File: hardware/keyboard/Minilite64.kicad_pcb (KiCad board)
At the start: 2 copper layers, 285.5 x 94.9 mm, 132 parts, among them J1 20P 1.0mm FFC ZIF bottom-cont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, SW1 Kailh MX hotswap / ~ / `, SW10 Kailh MX hotswap / ( / 9, SW11 Kailh MX hotswap / ) / 0, SW12 Kailh MX hotswap / _ / -, SW13 Kailh MX hotswap / + / =, SW14 Kailh MX hotswap / Backspace, SW15 Kailh MX hotswap / Tab, SW16 Kailh MX hotswap / Q, SW17 Kailh MX hotswap / W, SW18 Kailh MX hotswap / E, SW19 Kailh MX hotswap / R, SW2 Kailh MX hotswap / ! / 1, SW20 Kailh MX hotswap / T, SW21 Kailh MX hotswap / Y, SW22 Kailh MX hotswap / U, SW23 Kailh MX hotswap / I, SW24 Kailh MX hotswap / O, SW25 Kailh MX hotswap / P, SW26 Kailh MX hotswap / { / [, SW27 Kailh MX hotswap / } / ], SW28 Kailh MX hotswap / | / \, SW29 Kailh MX hotswap / Caps Lock, SW3 Kailh MX hotswap / @ / 2, SW30 Kailh MX hotswap / A, SW31 Kailh MX hotswap / S, SW32 Kailh MX hotswap / D, SW33 Kailh MX hotswap / F, SW34 Kailh MX hotswap / G, SW35 Kailh MX hotswap / H, SW36 Kailh MX hotswap / J, SW37 Kailh MX hotswap / K, SW38 Kailh MX hotswap / L, SW39 Kailh MX hotswap / : / ;, SW4 Kailh MX hotswap / # / 3, SW40 Kailh MX hotswap / " / ', SW41 Kailh MX hotswap / Enter, SW42 Kailh MX hotswap / Shift, SW43 Kailh MX hotswap / Z, SW44 Kailh MX hotswap / X, SW45 Kailh MX hotswap / C, SW46 Kailh MX hotswap / V, SW47 Kailh MX hotswap / B, SW48 Kailh MX hotswap / N, SW49 Kailh MX hotswap / M, SW5 Kailh MX hotswap / $ / 4, SW50 Kailh MX hotswap / < / ,, SW51 Kailh MX hotswap / > / ., SW52 Kailh MX hotswap / ? / /, SW53 Kailh MX hotswap / Shift, SW54 Kailh MX hotswap / Ctrl, SW55 Kailh MX hotswap / Win, SW56 Kailh MX hotswap / Alt, SW57 Kailh MX hotswap / Fn1, SW58 Kailh MX hotswap /, SW59 Kailh MX hotswap / Fn2, SW6 Kailh MX hotswap / % / 5, SW60 Kailh MX hotswap / Menu, SW61 Kailh MX hotswap / Fn3, SW62 Kailh MX hotswap / Alt, SW63 Kailh MX hotswap / Win, SW64 Kailh MX hotswap / Ctrl, SW7 Kailh MX hotswap / ^ / 6, SW8 Kailh MX hotswap / & / 7, SW9 Kailh MX hotswap / * / 8

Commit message: Add balanced bottom-row mounts and Case.step enclosure
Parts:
- added H4: M2 clearance, MountingHole_2.4mm, F.Cu at (47.6, 85.2)
- added H5: M2 clearance, MountingHole_2.4mm, F.Cu at (238.1, 85.2)
- H1, H2, H3: value M2.5 clearance -> M2 clearance
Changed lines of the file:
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@@
   (footprint "MountingHole_2.7mm" (layer "F.Cu") (at 25.575 28.2248)
     (property "Reference" "H1" (at 0 3.3 0) (layer "F.Fab") (effects (font (size 0.8 0.8) (thickness 0.12))))
-    (property "Value" "M2.5 clearance" (at 0 0 0) (layer "F.Fab") hide (effects (font (size 0.8 0.8) (thickness 0.12))))
+    (property "Value" "M2 clearance" (at 0 0 0) (layer "F.Fab") hide (effects (font (size 0.8 0.8) (thickness 0.12))))
     (pad "" np_thru_hole circle (at 0 0) (size 2.7 2.7) (drill 2.7) (layers "*.Cu" "*.Mask"))
   )
   (footprint "MountingHole_2.7mm" (layer "F.Cu") (at 128.576 47.6256)
     (property "Reference" "H2" (at 0 3.3 0) (layer "F.Fab") (effects (font (size 0.8 0.8) (thickness 0.12))))
-    (property "Value" "M2.5 clearance" (at 0 0 0) (layer "F.Fab") hide (effects (font (size 0.8 0.8) (thickness 0.12))))
+    (property "Value" "M2 clearance" (at 0 0 0) (layer "F.Fab") hide (effects (font (size 0.8 0.8) (thickness 0.12))))
     (pad "" np_thru_hole circle (at 0 0) (size 2.7 2.7) (drill 2.7) (layers "*.Cu" "*.Mask"))
   )
   (footprint "MountingHole_2.7mm" (layer "F.Cu") (at 260.4245 28.2248)
     (property "Reference" "H3" (at 0 3.3 0) (layer "F.Fab") (effects (font (size 0.8 0.8) (thickness 0.12))))
-    (property "Value" "M2.5 clearance" (at 0 0 0) (layer "F.Fab") hide (effects (font (size 0.8 0.8) (thickness 0.12))))
+    (property "Value" "M2 clearance" (at 0 0 0) (layer "F.Fab") hide (effects (font (size 0.8 0.8) (thickness 0.12))))
     (pad "" np_thru_hole circle (at 0 0) (size 2.7 2.7) (drill 2.7) (layers "*.Cu" "*.Mask"))
   )
+  (footprint "MountingHole_2.4mm" (layer "F.Cu") (at 47.625 85.2)
+    (property "Reference" "H4" (at 0 3.3 0) (layer "F.Fab") (effects (font (size 0.8 0.8) (thickness 0.12))))
+    (property "Value" "M2 clearance" (at 0 0 0) (layer "F.Fab") hide (effects (font (size 0.8 0.8) (thickness 0.12))))
+    (pad "" np_thru_hole circle (at 0 0) (size 2.4 2.4) (drill 2.4) (layers "*.Cu" "*.Mask"))
+  )
+  (footprint "MountingHole_2.4mm" (layer "F.Cu") (at 238.125 85.2)
+    (property "Reference" "H5" (at 0 3.3 0) (layer "F.Fab") (effects (font (size 0.8 0.8) (thickness 0.12))))
+    (property "Value" "M2 clearance" (at 0 0 0) (layer "F.Fab") hide (effects (font (size 0.8 0.8) (thickness 0.12))))
+    (pad "" np_thru_hole circle (at 0 0) (size 2.4 2.4) (drill 2.4) (layers "*.Cu" "*.Mask"))
+  )
   (gr_text "MINILITE64 • REV B • 2 LAYER" (at 142.875 92.2) (layer "F.SilkS") (effects (font (size 1 1) (thickness 0.18))))

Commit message: Add A1 plate fit-check and PCB verification silk
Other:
- board text added: "PLATE DXF • 1:1 CHECK"

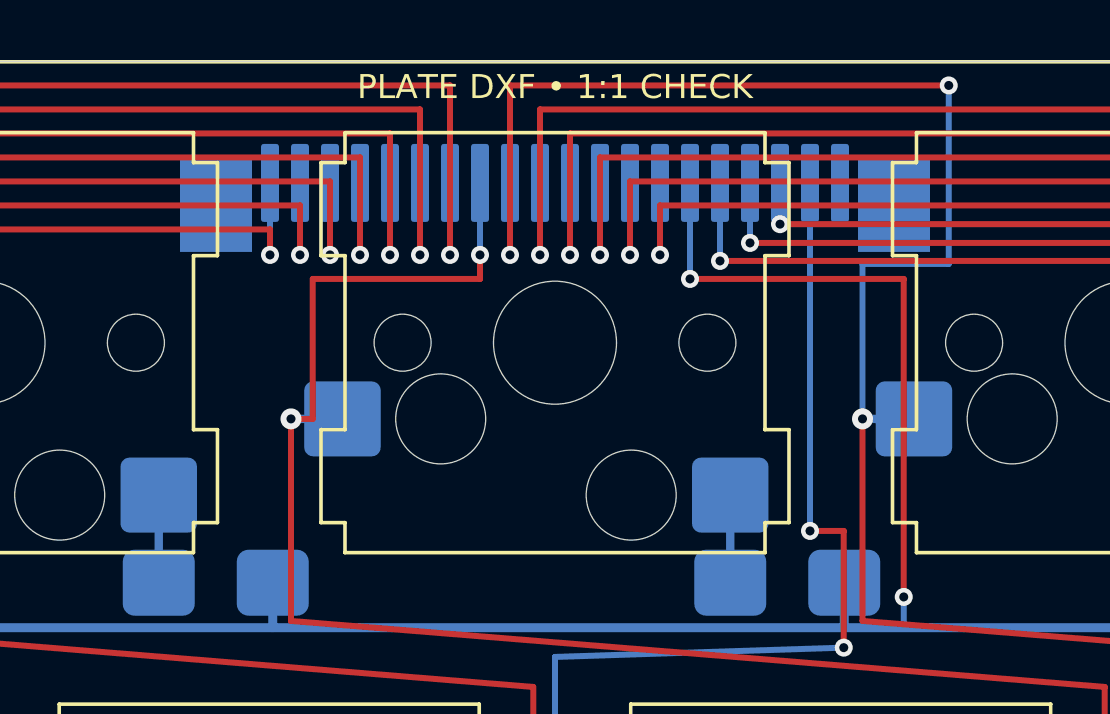
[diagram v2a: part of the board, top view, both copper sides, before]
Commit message: Finalize FFC routing and assembly-safe hardware
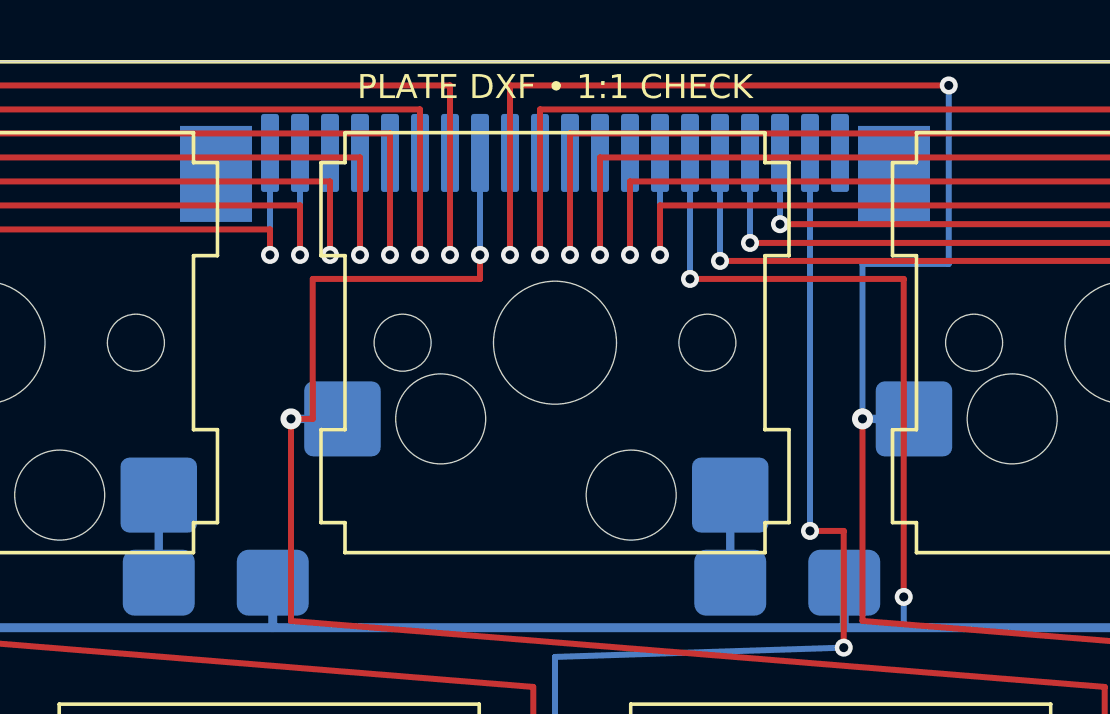
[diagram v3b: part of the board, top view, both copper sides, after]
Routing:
- net ROW4: track 407.0 -> 408.0 mm
- net ROW3: track 453.6 -> 454.6 mm
- net ROW2: track 422.6 -> 423.6 mm
- net ROW1: track 381.9 -> 382.9 mm
- net ROW0: track 300.1 -> 301.1 mm
- net COL9: track 194.4 -> 195.4 mm
- net COL8: track 179.1 -> 180.1 mm
- net COL7: track 154.2 -> 155.2 mm
- net COL6: track 181.3 -> 182.3 mm
- net COL5: track 196.1 -> 197.1 mm
- net COL4: track 192.3 -> 193.3 mm
- net COL3: track 205.3 -> 206.3 mm
- net COL2: track 225.2 -> 226.2 mm
- net COL13: track 160.4 -> 161.4 mm
- net COL12: track 169.8 -> 170.8 mm
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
